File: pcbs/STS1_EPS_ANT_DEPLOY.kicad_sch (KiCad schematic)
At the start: 2 parts, among them Q11 SI7272DP-T1-GE3, Q12 SI7272DP-T1-GE3

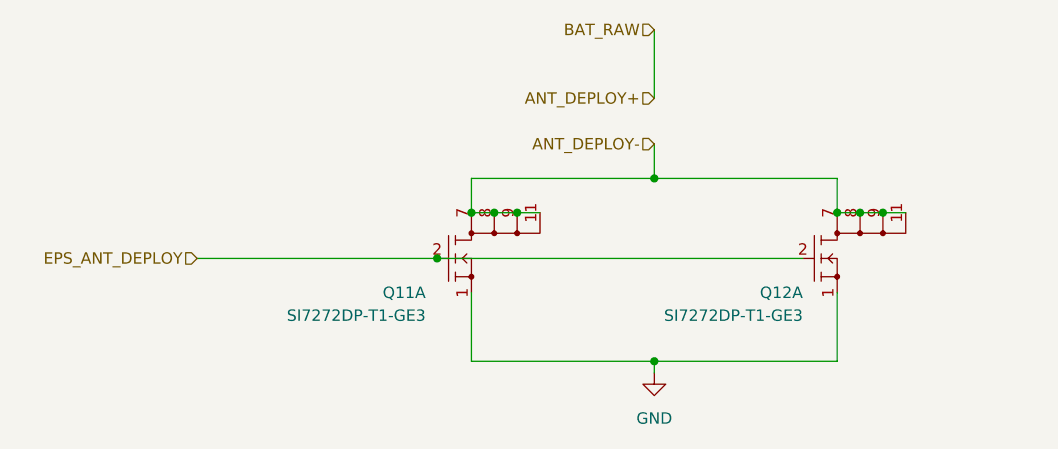
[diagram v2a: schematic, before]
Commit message: Cleared all DRC errors of STS1_EPS_1.
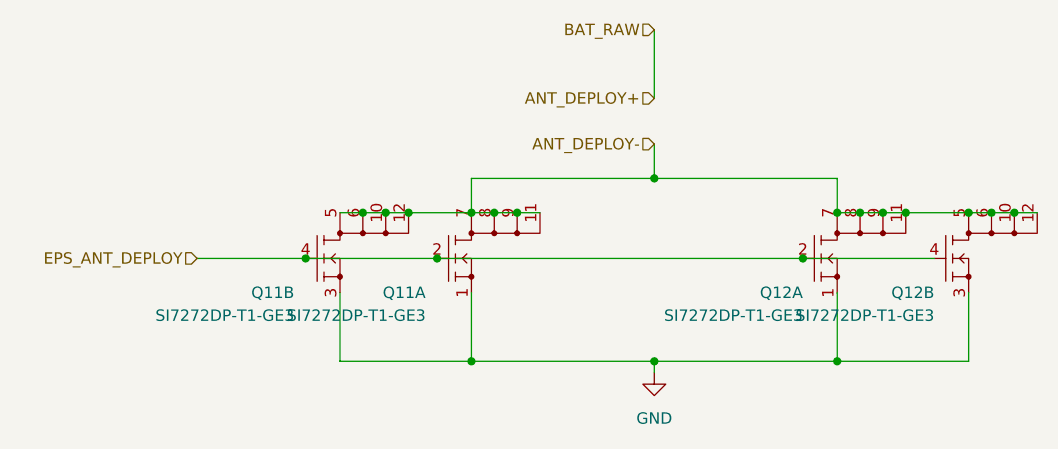
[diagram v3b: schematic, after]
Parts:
- added unit 2 of Q11
- added unit 2 of Q12
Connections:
- net ANT_DEPLOY-: now also Q11.10 (D2_3), Q11.12 (D2_4), Q11.5 (D2_1), Q11.6 (D2_2), Q12.10 (D2_3), Q12.12 (D2_4), Q12.5 (D2_1), Q12.6 (D2_2)
- net EPS_ANT_DEPLOY: now also Q11.4 (G2), Q12.4 (G2)
- net GND: now also Q11.3 (S2), Q12.3 (S2)
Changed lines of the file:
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@@
 (kicad_sch (version 20211123) (generator eeschema)
   (paper "A4")
+  (junction (at 53.975 93.98) (diameter 0) (color 0 0 0 0)
+  )
+  (junction (at 118.745 93.98) (diameter 0) (color 0 0 0 0)
+  )
   (junction (at 59.69 99.06) (diameter 0) (color 0 0 0 0)
   )
   (junction (at 83.82 110.49) (diameter 0) (color 0 0 0 0)
   )
+  (junction (at 63.5 110.49) (diameter 0) (color 0 0 0 0)
+  )
+  (junction (at 45.085 99.06) (diameter 0) (color 0 0 0 0)
+  )
+  (junction (at 104.14 110.49) (diameter 0) (color 0 0 0 0)
+  )
   (junction (at 106.68 93.98) (diameter 0) (color 0 0 0 0)
   )
   (junction (at 66.04 93.98) (diameter 0) (color 0 0 0 0)
   )
+  (junction (at 100.33 99.06) (diameter 0) (color 0 0 0 0)
+  )
+  (junction (at 56.515 93.98) (diameter 0) (color 0 0 0 0)
+  )
   (junction (at 109.22 93.98) (diameter 0) (color 0 0 0 0)
   )
@@
   (junction (at 83.82 90.17) (diameter 0) (color 0 0 0 0)
   )
+  (junction (at 111.76 93.98) (diameter 0) (color 0 0 0 0)
+  )
+  (junction (at 123.825 93.98) (diameter 0) (color 0 0 0 0)
+  )
   (junction (at 68.58 93.98) (diameter 0) (color 0 0 0 0)
   )
+  (junction (at 51.435 93.98) (diameter 0) (color 0 0 0 0)
+  )
+  (junction (at 121.285 93.98) (diameter 0) (color 0 0 0 0)
+  )
   (junction (at 104.14 93.98) (diameter 0) (color 0 0 0 0)
   )
+  (wire (pts (xy 48.895 102.87) (xy 48.895 110.49))
+    (stroke (width 0) (type default) (color 0 0 0 0))
+  )
+  (wire (pts (xy 51.435 93.98) (xy 53.975 93.98))
+    (stroke (width 0) (type default) (color 0 0 0 0))
+  )
+  (wire (pts (xy 100.33 99.06) (xy 114.935 99.06))
+    (stroke (width 0) (type default) (color 0 0 0 0))
+  )
   (wire (pts (xy 83.82 90.17) (xy 83.82 86.36))
     (stroke (width 0) (type default) (color 0 0 0 0))
@@
     (stroke (width 0) (type default) (color 0 0 0 0))
   )
+  (wire (pts (xy 45.085 99.06) (xy 59.69 99.06))
+    (stroke (width 0) (type default) (color 0 0 0 0))
+  )
   (wire (pts (xy 104.14 110.49) (xy 104.14 102.87))
     (stroke (width 0) (type default) (color 0 0 0 0))
@@
     (stroke (width 0) (type default) (color 0 0 0 0))
   )
+  (wire (pts (xy 118.745 93.98) (xy 121.285 93.98))
+    (stroke (width 0) (type default) (color 0 0 0 0))
+  )
+  (wire (pts (xy 53.975 93.98) (xy 56.515 93.98))
+    (stroke (width 0) (type default) (color 0 0 0 0))
+  )
   (wire (pts (xy 66.04 93.98) (xy 68.58 93.98))
     (stroke (width 0) (type default) (color 0 0 0 0))
@@
     (stroke (width 0) (type default) (color 0 0 0 0))
   )
+  (wire (pts (xy 56.515 93.98) (xy 63.5 93.98))
+    (stroke (width 0) (type default) (color 0 0 0 0))
+  )
   (wire (pts (xy 63.5 93.98) (xy 63.5 90.17))
     (stroke (width 0) (type default) (color 0 0 0 0))
@@
     (stroke (width 0) (type default) (color 0 0 0 0))
   )
-  (wire (pts (xy 33.02 99.06) (xy 59.69 99.06))
+  (wire (pts (xy 121.285 93.98) (xy 123.825 93.98))
+    (stroke (width 0) (type default) (color 0 0 0 0))
+  )
+  (wire (pts (xy 48.895 110.49) (xy 63.5 110.49))
+    (stroke (width 0) (type default) (color 0 0 0 0))
+  )
+  (wire (pts (xy 118.745 110.49) (xy 104.14 110.49))
+    (stroke (width 0) (type default) (color 0 0 0 0))
+  )
+  (wire (pts (xy 33.02 99.06) (xy 45.085 99.06))
     (stroke (width 0) (type default) (color 0 0 0 0))
   )
@@
     (stroke (width 0) (type default) (color 0 0 0 0))
   )
+  (wire (pts (xy 123.825 93.98) (xy 126.365 93.98))
+    (stroke (width 0) (type default) (color 0 0 0 0))
+  )
+  (wire (pts (xy 111.76 93.98) (xy 118.745 93.98))
+    (stroke (width 0) (type default) (color 0 0 0 0))
+  )
+  (wire (pts (xy 118.745 102.87) (xy 118.745 110.49))
+    (stroke (width 0) (type default) (color 0 0 0 0))
+  )
   (wire (pts (xy 104.14 90.17) (xy 104.14 93.98))
     (stroke (width 0) (type default) (color 0 0 0 0))
@@
   )
   (wire (pts (xy 83.82 110.49) (xy 104.14 110.49))
+    (stroke (width 0) (type default) (color 0 0 0 0))
+  )
+  (wire (pts (xy 48.895 93.98) (xy 51.435 93.98))
     (stroke (width 0) (type default) (color 0 0 0 0))
   )
@@
     (pin "6")
   )
+  (symbol (lib_id "STS_Transistor_FET:SI7272DP-T1-GE3") (at 114.935 99.06 0) (unit 2)
+    (in_bom yes) (on_board yes)
+    (property "Reference" "Q12" (id 0) (at 114.935 102.87 0)
+      (effects (font (size 1.27 1.27)) (justify right))
+    )
+    (property "Value" "SI7272DP-T1-GE3" (id 1) (at 114.935 105.41 0)
+      (effects (font (size 1.27 1.27)) (justify right))
+    )
+    (property "Footprint" "STS_Package_SO:POWERPAK_SO8" (id 2) (at 120.777 100.33 0)
+      (effects (font (size 1.27 1.27)) (justify left) hide)
+    )
+    (property "Datasheet" "" (id 3) (at 165.735 99.06 0)
+      (effects (font (size 1.27 1.27)) (justify left) hide)
+    )
+    (property "Manufacturer_Name" "Vishay" (id 4) (at 121.031 103.632 0)
+      (effects (font (size 1.27 1.27)) (justify left) hide)
+    )
+    (pin "1")
+    (pin "11")
+    (pin "2")
+    (pin "2")
+    (pin "7")
+    (pin "8")
+    (pin "9")
+    (pin "10")
+    (pin "12")
+    (pin "3")
+    (pin "4")
+    (pin "5")
+    (pin "6")
+  )
   (symbol (lib_id "STS_Transistor_FET:SI7272DP-T1-GE3") (at 59.69 99.06 0) (unit 1)
     (in_bom yes) (on_board yes)
@@
       (effects (font (size 1.27 1.27)) (justify left) hide)
     )
+    (pin "1")
+    (pin "11")
+    (pin "2")
+    (pin "2")
+    (pin "7")
+    (pin "8")
+    (pin "9")
+    (pin "10")
+    (pin "12")
+    (pin "3")
+    (pin "4")
+    (pin "5")
+    (pin "6")
+  )
+  (symbol (lib_id "STS_Transistor_FET:SI7272DP-T1-GE3") (at 45.085 99.06 0) (unit 2)
+    (in_bom yes) (on_board yes)
+    (property "Reference" "Q11" (id 0) (at 43.815 102.87 0)
+      (effects (font (size 1.27 1.27)) (justify right))
+    )
+    (property "Value" "SI7272DP-T1-GE3" (id 1) (at 43.815 105.41 0)
+      (effects (font (size 1.27 1.27)) (justify right))
+    )
+    (property "Footprint" "STS_Package_SO:POWERPAK_SO8" (id 2) (at 50.927 100.33 0)
+      (effects (font (size 1.27 1.27)) (justify left) hide)
+    )
+    (property "Datasheet" "" (id 3) (at 95.885 99.06 0)
+      (effects (font (size 1.27 1.27)) (justify left) hide)
+    )
+    (property "Manufacturer_Name" "Vishay" (id 4) (at 51.181 103.632 0)
+      (effects (font (size 1.27 1.27)) (justify left) hide)
+    )

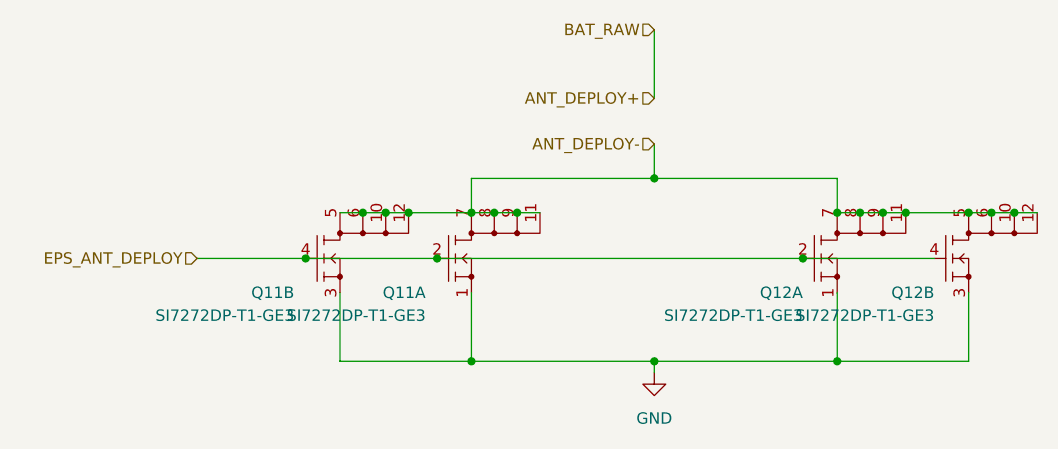
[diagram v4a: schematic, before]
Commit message: Added test points to STS1_EPS_2.
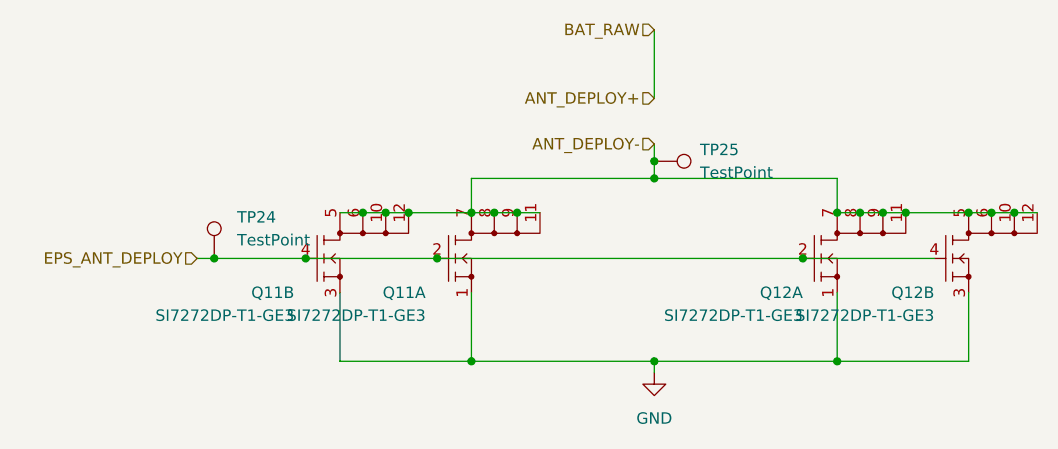
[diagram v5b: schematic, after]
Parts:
- added TP24, TP25: TestPoint, TestPoint:TestPoint_THTPad_D1.0mm_Drill0.5mm, symbol Connector:TestPoint
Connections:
- net ANT_DEPLOY-: now also TP25.1
- net EPS_ANT_DEPLOY: now also TP24.1
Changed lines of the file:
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@@
   (junction (at 83.82 110.49) (diameter 0) (color 0 0 0 0)
   )
+  (junction (at 34.925 99.06) (diameter 0) (color 0 0 0 0)
+  )
   (junction (at 63.5 110.49) (diameter 0) (color 0 0 0 0)
   )
   (junction (at 45.085 99.06) (diameter 0) (color 0 0 0 0)
   )
+  (junction (at 83.82 88.265) (diameter 0) (color 0 0 0 0)
+  )
   (junction (at 104.14 110.49) (diameter 0) (color 0 0 0 0)
   )
@@
     (stroke (width 0) (type default) (color 0 0 0 0))
   )
-  (wire (pts (xy 83.82 90.17) (xy 83.82 86.36))
+  (wire (pts (xy 83.82 90.17) (xy 83.82 88.265))
     (stroke (width 0) (type default) (color 0 0 0 0))
   )
@@
     (stroke (width 0) (type default) (color 0 0 0 0))
   )
+  (wire (pts (xy 34.925 99.06) (xy 45.085 99.06))
+    (stroke (width 0) (type default) (color 0 0 0 0))
+  )
   (wire (pts (xy 53.975 93.98) (xy 56.515 93.98))
     (stroke (width 0) (type default) (color 0 0 0 0))
@@
     (stroke (width 0) (type default) (color 0 0 0 0))
   )
+  (wire (pts (xy 83.82 88.265) (xy 83.82 86.36))
+    (stroke (width 0) (type default) (color 0 0 0 0))
+  )
   (wire (pts (xy 83.82 73.66) (xy 83.82 81.28))
     (stroke (width 0) (type default) (color 0 0 0 0))
@@
     (stroke (width 0) (type default) (color 0 0 0 0))
   )
-  (wire (pts (xy 33.02 99.06) (xy 45.085 99.06))
+  (wire (pts (xy 33.02 99.06) (xy 34.925 99.06))
     (stroke (width 0) (type default) (color 0 0 0 0))
   )
@@
     (pin "6")
   )
+  (symbol (lib_id "Connector:TestPoint") (at 83.82 88.265 270) (unit 1)
+    (in_bom yes) (on_board yes) (fields_autoplaced)
+    (property "Reference" "TP25" (id 0) (at 88.9 86.9949 90)
+      (effects (font (size 1.27 1.27)) (justify left))
+    )
+    (property "Value" "TestPoint" (id 1) (at 88.9 89.5349 90)
+      (effects (font (size 1.27 1.27)) (justify left))
+    )
+    (property "Footprint" "TestPoint:TestPoint_THTPad_D1.0mm_Drill0.5mm" (id 2) (at 83.82 93.345 0)
+      (effects (font (size 1.27 1.27)) hide)
+    )
+    (property "Datasheet" "~" (id 3) (at 83.82 93.345 0)
+      (effects (font (size 1.27 1.27)) hide)
+    )
+    (pin "1")
+  )
+  (symbol (lib_id "Connector:TestPoint") (at 34.925 99.06 0) (unit 1)
+    (in_bom yes) (on_board yes) (fields_autoplaced)
+    (property "Reference" "TP24" (id 0) (at 37.465 94.4879 0)
+      (effects (font (size 1.27 1.27)) (justify left))
+    )
+    (property "Value" "TestPoint" (id 1) (at 37.465 97.0279 0)
+      (effects (font (size 1.27 1.27)) (justify left))
+    )
+    (property "Footprint" "TestPoint:TestPoint_THTPad_D1.0mm_Drill0.5mm" (id 2) (at 40.005 99.06 0)
+      (effects (font (size 1.27 1.27)) hide)
+    )
+    (property "Datasheet" "~" (id 3) (at 40.005 99.06 0)
+      (effects (font (size 1.27 1.27)) hide)
+    )
+    (pin "1")
+  )
   (symbol (lib_id "power:GND") (at 83.82 111.76 0) (unit 1)

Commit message: Worked on STS1_EPS_2.
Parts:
- renumbered Q11 to Q21, Q12 to Q22
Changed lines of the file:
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@@
   (symbol (lib_id "STS_Transistor_FET:SI7272DP-T1-GE3") (at 100.33 99.06 0) (unit 1)
     (in_bom yes) (on_board yes)
-    (property "Reference" "Q12" (id 0) (at 100.33 102.87 0)
+    (property "Reference" "Q22" (id 0) (at 100.33 102.87 0)
       (effects (font (size 1.27 1.27)) (justify right))
     )
@@
   (symbol (lib_id "STS_Transistor_FET:SI7272DP-T1-GE3") (at 114.935 99.06 0) (unit 2)
     (in_bom yes) (on_board yes)
-    (property "Reference" "Q12" (id 0) (at 114.935 102.87 0)
+    (property "Reference" "Q22" (id 0) (at 114.935 102.87 0)
       (effects (font (size 1.27 1.27)) (justify right))
     )
@@
   (symbol (lib_id "STS_Transistor_FET:SI7272DP-T1-GE3") (at 59.69 99.06 0) (unit 1)
     (in_bom yes) (on_board yes)
-    (property "Reference" "Q11" (id 0) (at 58.42 102.87 0)
+    (property "Reference" "Q21" (id 0) (at 58.42 102.87 0)
       (effects (font (size 1.27 1.27)) (justify right))
     )
@@
   (symbol (lib_id "STS_Transistor_FET:SI7272DP-T1-GE3") (at 45.085 99.06 0) (unit 2)
     (in_bom yes) (on_board yes)
-    (property "Reference" "Q11" (id 0) (at 43.815 102.87 0)
+    (property "Reference" "Q21" (id 0) (at 43.815 102.87 0)
       (effects (font (size 1.27 1.27)) (justify right))
     )
@@
   (symbol (lib_id "power:GND") (at 83.82 111.76 0) (unit 1)
     (in_bom yes) (on_board yes) (fields_autoplaced)
-    (property "Reference" "#PWR018" (id 0) (at 83.82 118.11 0)
+    (property "Reference" "#PWR070" (id 0) (at 83.82 118.11 0)
       (effects (font (size 1.27 1.27)) hide)
     )
